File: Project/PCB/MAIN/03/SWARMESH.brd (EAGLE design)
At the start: 75 x 75 mm, 48 parts, among them Q1 TIP122, U1 ESP32DEVKITC, U2 CD4051BEE4, U3 L293D, U4 L7805CV-DG, U5 TCRT5000L, U6 TCRT5000L

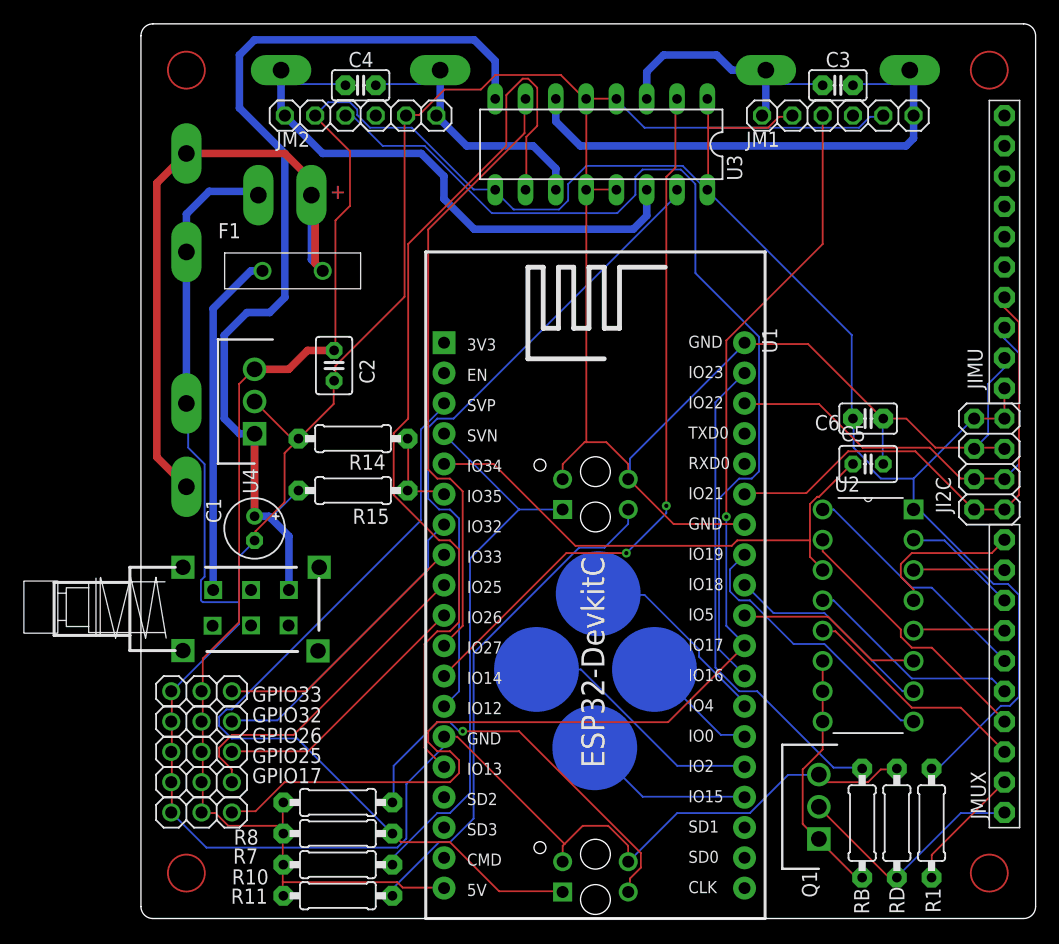
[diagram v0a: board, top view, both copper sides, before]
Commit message: added power net to PCB, corrected orphan GND network in SCH
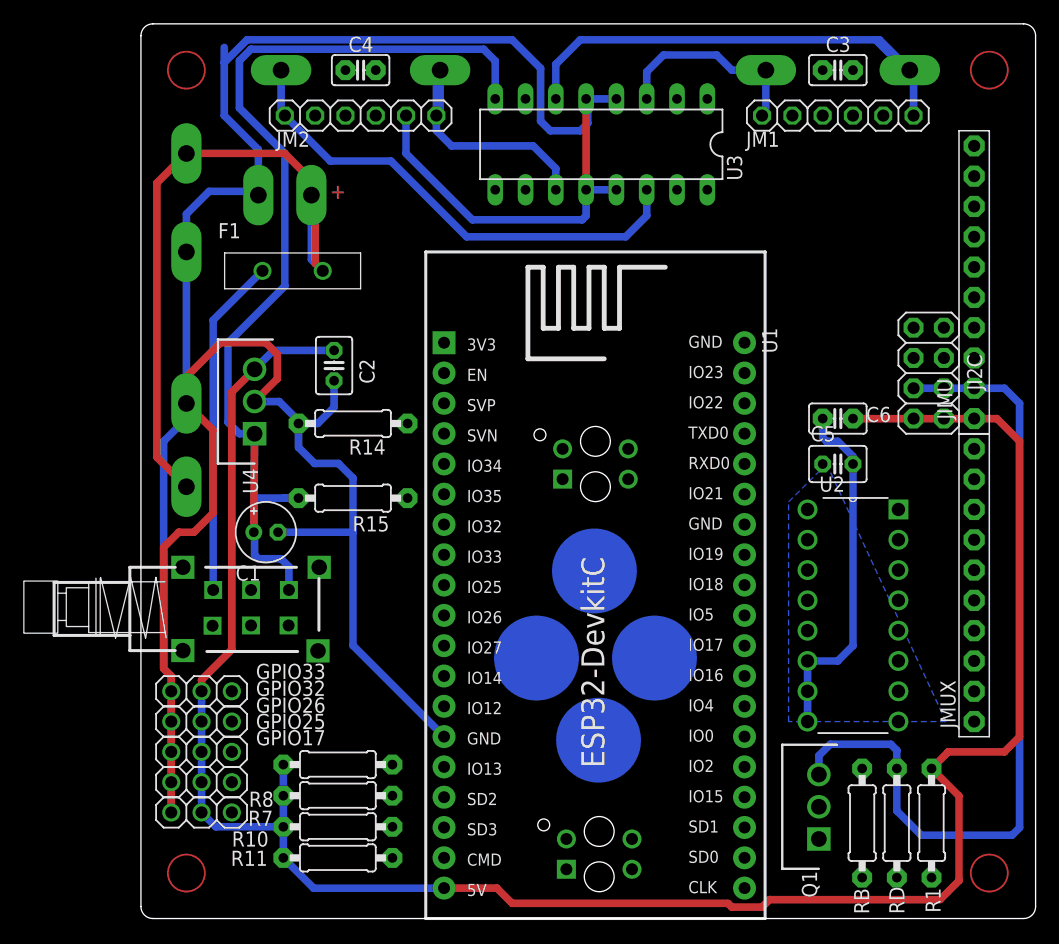
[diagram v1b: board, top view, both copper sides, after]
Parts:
- moved JI2C 9.16 mm to (66.0, 45.7), turned to 90 degrees
- moved JMUX 8.03 mm to (69.8, 27.9)
- moved JIMU 3.59 mm to (69.8, 53.3)
- moved R10 3.17 mm to (16.5, 7.69)
- moved R11 3.17 mm to (16.5, 5.08)
- moved R7 3.17 mm to (16.5, 10.3)
- moved R8 3.17 mm to (16.5, 12.9)
- moved C5 2.54 mm to (58.4, 38.1)
- moved C6 2.54 mm to (58.4, 41.9), turned to 180 degrees
- moved U6 2.54 mm to (38.1, 38.1)
- moved T4 1.93 mm to (38.0, 29.1)
- moved U5 1.93 mm to (38.4, 5.40)
- moved C3 1.27 mm to (58.4, 71.1)
- moved C4 1.27 mm to (18.4, 71.1)
- moved R14 1.27 mm to (17.8, 41.5)
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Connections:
- removed net N$12: Q1.1, RB.1, U2.6, U2.7, U2.8
- new net N$1: Q1.1, RB.1
- net GND: now also U2.6, U2.7, U2.8
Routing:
- net E1A: track 103.6 -> 0.00 mm, vias 1 -> 0
- net E2A: track 82.0 -> 0.00 mm
- net IO13: track 78.0 -> 0.00 mm
- net IR1: track 69.7 -> 0.00 mm
- net IO14: track 59.4 -> 0.00 mm, vias 2 -> 0
- net IO12: track 54.9 -> 0.00 mm
- net VCC: track 231.5 -> 179.1 mm
- net IO27: track 51.7 -> 0.00 mm
- net IR2: track 47.4 -> 0.00 mm
- net ADCMX: track 44.7 -> 0.00 mm
- net SDA: track 44.1 -> 0.00 mm
- net N$9: track 42.4 -> 0.00 mm
- net IRTX: track 41.5 -> 0.00 mm
- net SCL: track 38.2 -> 0.00 mm
- net N$10: track 33.7 -> 0.00 mm, vias 1 -> 0
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- added copper zone on layer 16, net GND
